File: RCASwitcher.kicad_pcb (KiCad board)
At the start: 2 copper layers, 11 parts, among them J1 Connector_RCA_2x3_REB, J2 Connector_RCA_2x3_REB, J3 Connector_RCA_2x3_REB, J4 Connector_RCA_2x3_REB, J5 Connector_RCA_2x3_REB, J6 Connector_RCA_2x3_REB, SW1 SW_SPDT_3x2_REB, SW2 SW_SPDT_3x2_REB, SW3 SW_SPDT_3x2_REB, SW4 SW_SPDT_3x2_REB, SW5 SW_SPDT_3x2_REB

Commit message: Removing ignored files, some layout
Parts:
- J1, J3, J6: moved to B.Cu
- moved J1 216.2 mm to (49.2, 86.5), turned to 180 degrees
- moved J4 169.1 mm to (99.8, 74.5)
- moved J2 160.8 mm to (56.8, 74.5)
- moved J6 128.2 mm to (135.2, 86.5), turned to 180 degrees
- moved J3 123.3 mm to (92.2, 86.5), turned to 180 degrees
- moved J5 69.1 mm to (142.8, 74.5)
- moved SW4 24.6 mm to (108.8, 138.0)
- moved SW5 24.5 mm to (124.8, 138.0)
- moved SW3 24.1 mm to (93.8, 138.0)
- moved SW2 23.4 mm to (78.8, 138.0)
- moved SW1 23.1 mm to (63.8, 138.0)
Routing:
- net /GND_out: track 0.00 -> 133.4 mm
- net /L_out: track 0.00 -> 133.2 mm
- net Net-(J1-Pad7): track 0.00 -> 131.3 mm
- net /Y_out: track 0.00 -> 131.0 mm
- net Net-(J3-Pad7): track 0.00 -> 112.8 mm
- net /Pb_out: track 0.00 -> 111.1 mm
- net /R_out: track 0.00 -> 110.7 mm
- net Net-(J1-Pad4): track 0.00 -> 109.5 mm
- net Net-(J2-Pad4): track 0.00 -> 103.9 mm, vias 0 -> 1
- net Net-(J1-Pad1): track 0.00 -> 103.2 mm
- net /Pr_out: track 0.00 -> 95.3 mm
- net Net-(J3-Pad4): track 0.00 -> 92.1 mm
- net Net-(J2-Pad1): track 0.00 -> 88.4 mm, vias 0 -> 1
- net Net-(J3-Pad1): track 0.00 -> 86.1 mm
- net Net-(J1-Pad5): track 0.00 -> 85.4 mm, vias 0 -> 1
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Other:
- board outline added: 128.5 x 75.5 mm

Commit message: finish hookups
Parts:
- J5: moved to B.Cu
- J6: moved to F.Cu
- moved J5 14.2 mm to (135.2, 86.5), turned to 180 degrees
- moved J6 14.2 mm to (142.8, 74.5), turned to 0 degrees
- moved SW5 1.00 mm to (123.8, 138.0)
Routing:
- net Net-(J4-Pad4): track 0.00 -> 90.6 mm, vias 0 -> 1
- net Net-(J4-Pad1): track 0.00 -> 74.2 mm, vias 0 -> 1
- net Net-(J5-Pad1): track 0.00 -> 70.9 mm
- net Net-(J4-Pad5): track 0.00 -> 69.0 mm, vias 0 -> 1
- net Net-(J5-Pad4): track 0.00 -> 62.5 mm
- net Net-(J4-Pad2): track 0.00 -> 59.0 mm, vias 0 -> 1
- net Net-(J5-Pad2): track 0.00 -> 53.1 mm
- net /Pr_out: track 95.3 -> 145.1 mm
- net Net-(J4-Pad7): track 28.0 -> 77.4 mm
- net Net-(J4-Pad3): track 0.00 -> 46.7 mm, vias 0 -> 1
- net Net-(J5-Pad5): track 0.00 -> 44.7 mm
- net Net-(J5-Pad3): track 0.00 -> 41.8 mm
- net Net-(J5-Pad7): track 28.0 -> 65.4 mm
- net /Pb_out: track 111.1 -> 130.7 mm
- net /R_out: track 110.7 -> 119.4 mm
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
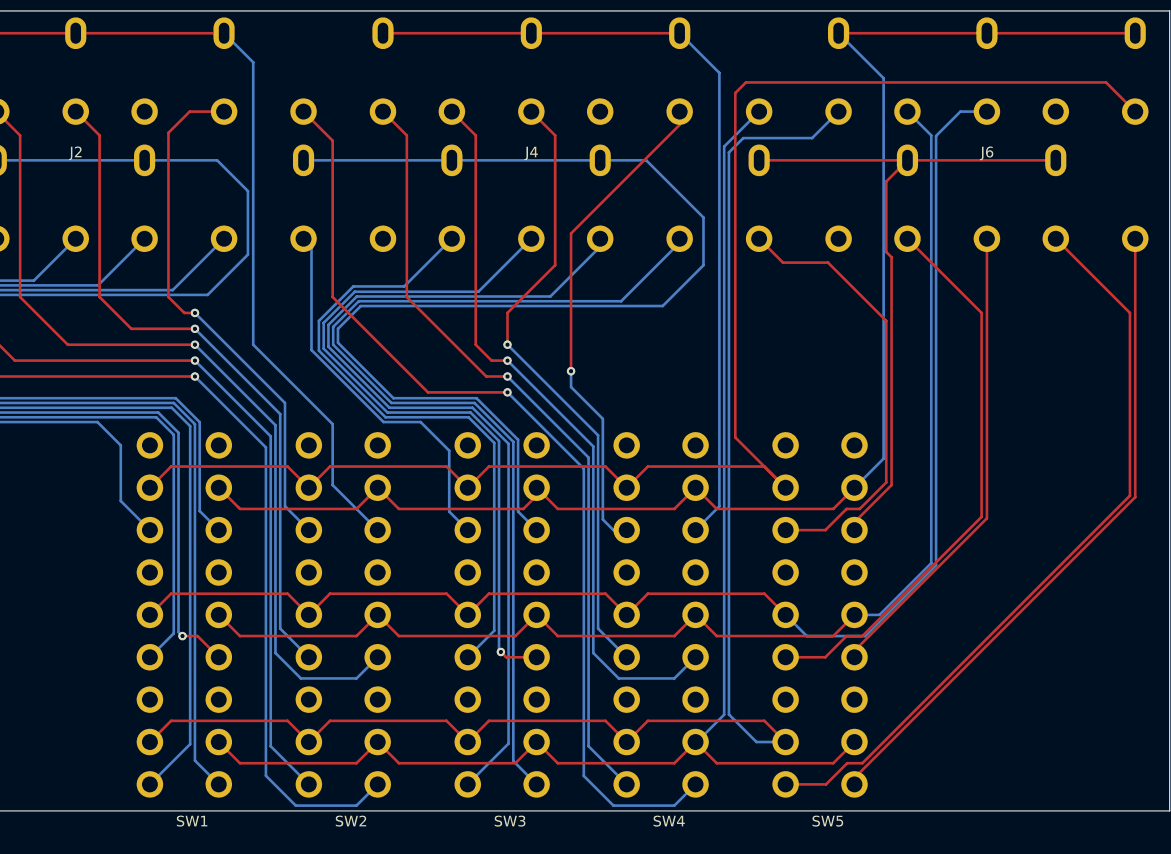
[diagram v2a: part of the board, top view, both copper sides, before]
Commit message: Name remaining nets for checking
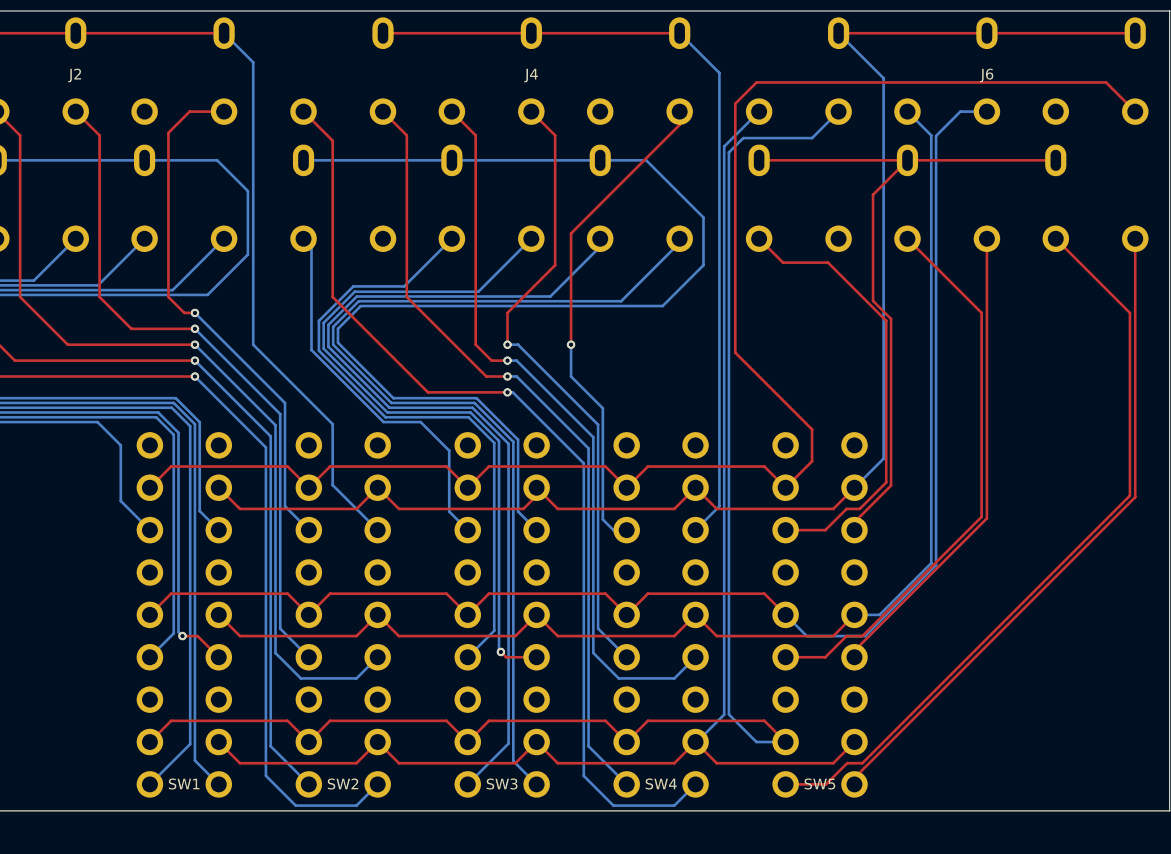
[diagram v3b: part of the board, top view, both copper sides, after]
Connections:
- net Net-(J1-Pad1) renamed /Y_1
- net Net-(J1-Pad2) renamed /Pb_1
- net Net-(J1-Pad3) renamed /Pr_1
- net Net-(J1-Pad4) renamed /L_1
- net Net-(J1-Pad5) renamed /R_1
- net Net-(J1-Pad7) renamed /GND_1
- net Net-(J2-Pad1) renamed /Y_2
- net Net-(J2-Pad2) renamed /Pb_2
- net Net-(J2-Pad3) renamed /Pr_2
- net Net-(J2-Pad4) renamed /L_2
- net Net-(J2-Pad5) renamed /R_2
- net Net-(J2-Pad7) renamed /GND_2
- net Net-(J3-Pad1) renamed /Y_3
- net Net-(J3-Pad2) renamed /Pb_3
- net Net-(J3-Pad3) renamed /Pr_3
- net Net-(J3-Pad4) renamed /L_3
- net Net-(J3-Pad5) renamed /R_3
- net Net-(J3-Pad7) renamed /GND_3
- net Net-(J4-Pad1) renamed /Y_4
- net Net-(J4-Pad2) renamed /Pb_4
- net Net-(J4-Pad3) renamed /Pr_4
- net Net-(J4-Pad4) renamed /L_4
- net Net-(J4-Pad5) renamed /R_4
- net Net-(J4-Pad7) renamed /GND_4
- net Net-(J5-Pad1) renamed /Y_5
- net Net-(J5-Pad2) renamed /Pb_5
- net Net-(J5-Pad3) renamed /Pr_5
- net Net-(J5-Pad4) renamed /L_5
- net Net-(J5-Pad5) renamed /R_5
- net Net-(J5-Pad7) renamed /GND_5
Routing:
- net /Pr_out: track 145.1 -> 146.6 mm
- net /GND_5: track 65.4 -> 66.4 mm
- net /Pb_4: track 59.0 -> 59.5 mm
- net /Y_4: track 74.2 -> 74.7 mm
- net /R_4: track 69.0 -> 69.5 mm

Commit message: Adds notes, one big mistake with switch must fix
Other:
- board text added: "Check whether upper or lower pad is NC when off! Designed with front = ON back = OFF OH NO! front = OFF back = ON Must redo this"
- board text added: "Double check pin assignments in correct orientations Towards front is upside down"
- board text added: "Print out and test spacing on paper!"
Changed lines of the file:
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@@
   )
   (gr_rect (start 31.5 65) (end 160 140.5) (layer "Edge.Cuts") (width 0.1) (fill none))
+  (gr_text "Print out and test spacing on paper!" (at 36.5 58) (layer "User.1")
+    (effects (font (size 1 1) (thickness 0.15)) (justify left))
+  )
+  (gr_text "Double check pin assignments in correct orientations\nTowards front is upside down" (at 33.5 83) (layer "User.1")
+    (effects (font (size 1 1) (thickness 0.15)) (justify left))
+  )
+  (gr_text "Check whether upper or lower\npad is NC when off!\nDesigned with front = ON back = OFF\nOH NO! front = OFF back = ON\nMust redo this" (at 60 134) (layer "User.1")
+    (effects (font (size 1 1) (thickness 0.15)) (justify right))
+  )
   (segment (start 39.359188 102.45) (end 65.813604 102.45) (width 0.25) (layer "B.Cu") (net 1))
   (segment (start 67.55 104.186396) (end 67.55 134.2) (width 0.25) (layer "B.Cu") (net 1))

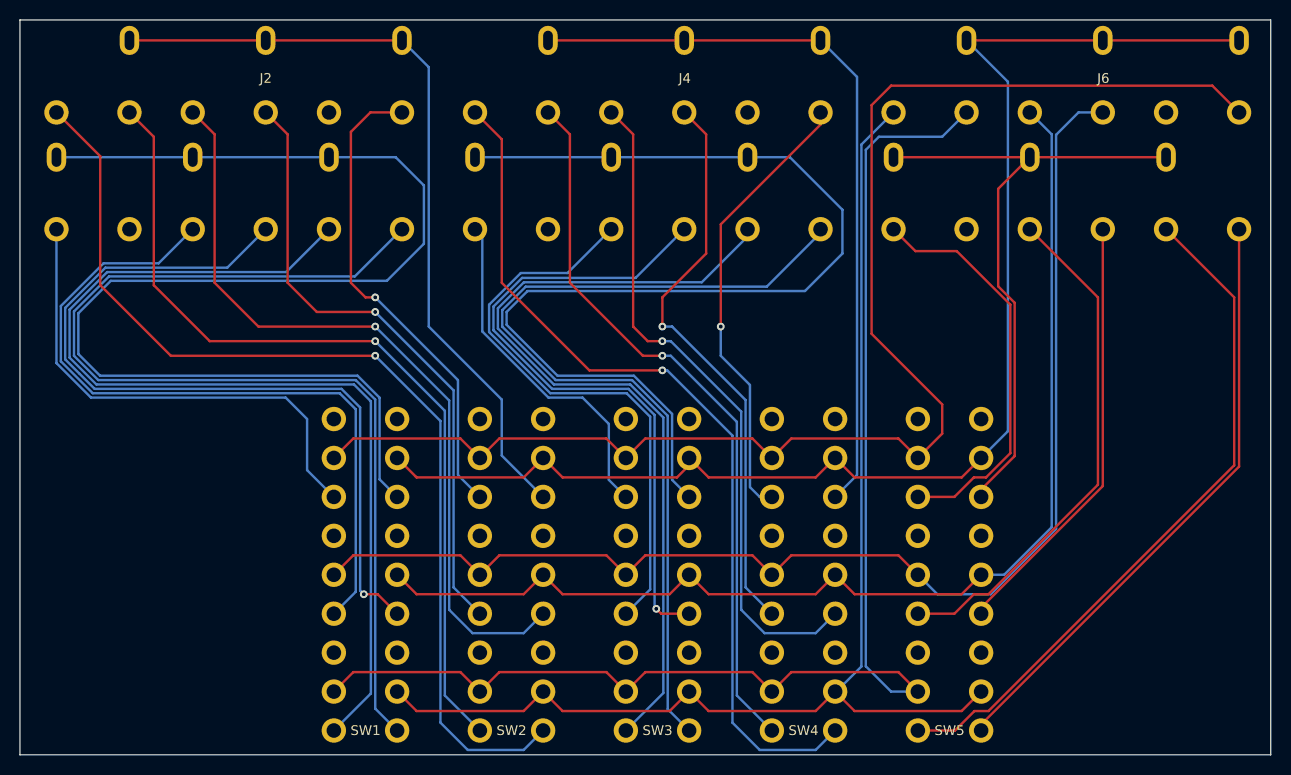
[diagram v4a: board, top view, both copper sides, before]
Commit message: Reversing which side gets connected, tested with hand soldering
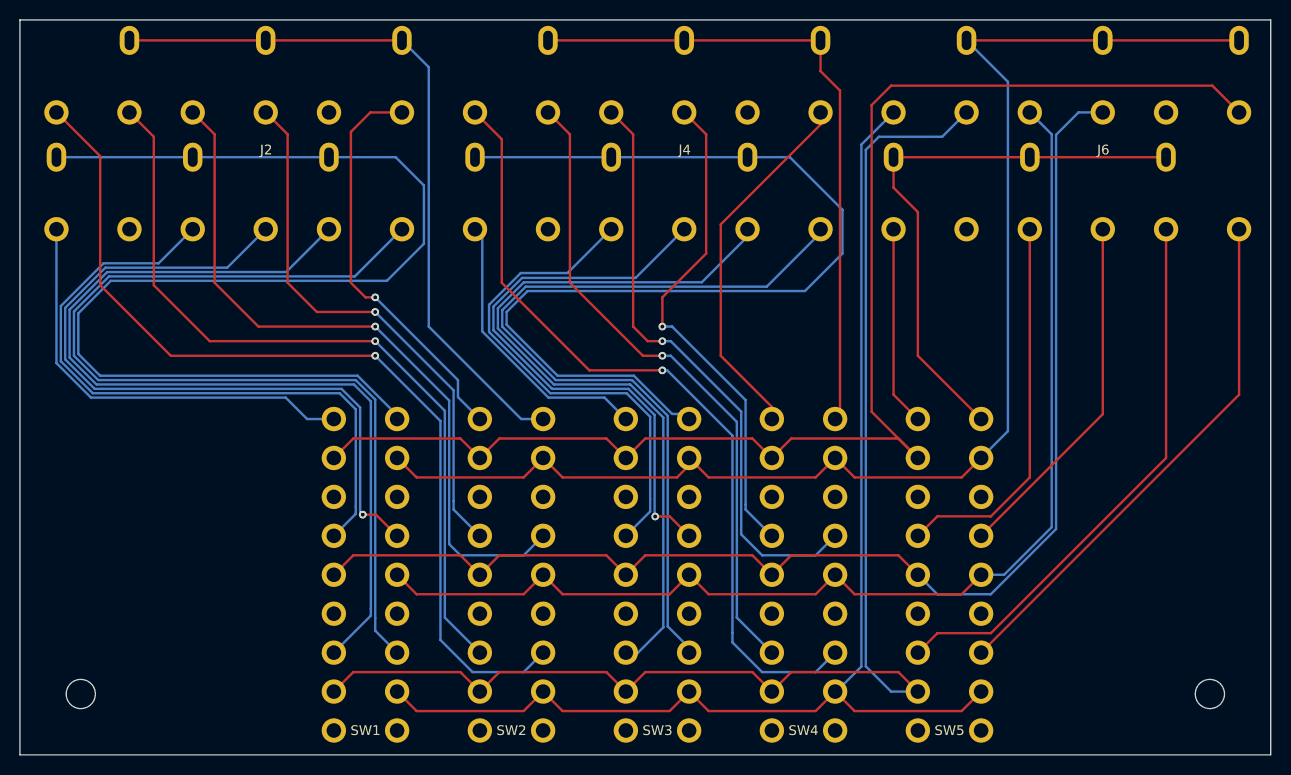
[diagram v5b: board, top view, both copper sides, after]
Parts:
- added REF**: MountingHole_3mm, MountingHole:MountingHole_3mm, F.Cu at (37.8, 134.2)
- added REF**: MountingHole_3mm, MountingHole:MountingHole_3mm, F.Cu at (153.8, 134.2)
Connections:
- SW1 pad 1: /Y_1 -> unconnected-(SW1-Pad1)
- SW1 pad 10: /L_1 -> unconnected-(SW1-Pad10)
- SW1 pad 12: unconnected-(SW1-Pad12) -> /L_1
- SW1 pad 13: /R_1 -> unconnected-(SW1-Pad13)
- SW1 pad 15: unconnected-(SW1-Pad15) -> /R_1
- SW1 pad 16: /GND_1 -> unconnected-(SW1-Pad16)
- SW1 pad 18: unconnected-(SW1-Pad18) -> /GND_1
- SW1 pad 3: unconnected-(SW1-Pad3) -> /Y_1
- SW1 pad 4: /Pb_1 -> unconnected-(SW1-Pad4)
- SW1 pad 6: unconnected-(SW1-Pad6) -> /Pb_1
- SW1 pad 7: /Pr_1 -> unconnected-(SW1-Pad7)
- SW1 pad 9: unconnected-(SW1-Pad9) -> /Pr_1
- SW2 pad 1: /Y_2 -> unconnected-(SW2-Pad1)
- SW2 pad 10: /L_2 -> unconnected-(SW2-Pad10)
- SW2 pad 12: unconnected-(SW2-Pad12) -> /L_2
- SW2 pad 13: /R_2 -> unconnected-(SW2-Pad13)
- SW2 pad 15: unconnected-(SW2-Pad15) -> /R_2
- SW2 pad 16: /GND_2 -> unconnected-(SW2-Pad16)
- SW2 pad 18: unconnected-(SW2-Pad18) -> /GND_2
- SW2 pad 3: unconnected-(SW2-Pad3) -> /Y_2
- SW2 pad 4: /Pb_2 -> unconnected-(SW2-Pad4)
- SW2 pad 6: unconnected-(SW2-Pad6) -> /Pb_2
- SW2 pad 7: /Pr_2 -> unconnected-(SW2-Pad7)
- SW2 pad 9: unconnected-(SW2-Pad9) -> /Pr_2
- SW3 pad 1: /Y_3 -> unconnected-(SW3-Pad1)
- SW3 pad 10: /L_3 -> unconnected-(SW3-Pad10)
- SW3 pad 12: unconnected-(SW3-Pad12) -> /L_3
- SW3 pad 13: /R_3 -> unconnected-(SW3-Pad13)
- SW3 pad 15: unconnected-(SW3-Pad15) -> /R_3
- SW3 pad 16: /GND_3 -> unconnected-(SW3-Pad16)
- SW3 pad 18: unconnected-(SW3-Pad18) -> /GND_3
- SW3 pad 3: unconnected-(SW3-Pad3) -> /Y_3
- SW3 pad 4: /Pb_3 -> unconnected-(SW3-Pad4)
- SW3 pad 6: unconnected-(SW3-Pad6) -> /Pb_3
- SW3 pad 7: /Pr_3 -> unconnected-(SW3-Pad7)
- SW3 pad 9: unconnected-(SW3-Pad9) -> /Pr_3
- SW4 pad 1: /Y_4 -> unconnected-(SW4-Pad1)
- SW4 pad 10: /L_4 -> unconnected-(SW4-Pad10)
- SW4 pad 12: unconnected-(SW4-Pad12) -> /L_4
- SW4 pad 13: /R_4 -> unconnected-(SW4-Pad13)
- SW4 pad 15: unconnected-(SW4-Pad15) -> /R_4
- SW4 pad 16: /GND_4 -> unconnected-(SW4-Pad16)
- SW4 pad 18: unconnected-(SW4-Pad18) -> /GND_4
- SW4 pad 3: unconnected-(SW4-Pad3) -> /Y_4
- SW4 pad 4: /Pb_4 -> unconnected-(SW4-Pad4)
- SW4 pad 6: unconnected-(SW4-Pad6) -> /Pb_4
- SW4 pad 7: /Pr_4 -> unconnected-(SW4-Pad7)
- SW4 pad 9: unconnected-(SW4-Pad9) -> /Pr_4
- SW5 pad 1: /Y_5 -> unconnected-(SW5-Pad1)
- SW5 pad 10: /L_5 -> unconnected-(SW5-Pad10)
- SW5 pad 12: unconnected-(SW5-Pad12) -> /L_5
- SW5 pad 13: /R_5 -> unconnected-(SW5-Pad13)
- SW5 pad 15: unconnected-(SW5-Pad15) -> /R_5
- SW5 pad 16: /GND_5 -> unconnected-(SW5-Pad16)
- SW5 pad 18: unconnected-(SW5-Pad18) -> /GND_5
- SW5 pad 3: unconnected-(SW5-Pad3) -> /Y_5
- SW5 pad 4: /Pb_5 -> unconnected-(SW5-Pad4)
- SW5 pad 6: unconnected-(SW5-Pad6) -> /Pb_5
- SW5 pad 7: /Pr_5 -> unconnected-(SW5-Pad7)
- SW5 pad 9: unconnected-(SW5-Pad9) -> /Pr_5
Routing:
- net /Pr_5: track 41.8 -> 20.5 mm
- net /Pb_5: track 53.1 -> 39.5 mm
- net /Y_5: track 70.9 -> 57.3 mm
- net /GND_4: track 77.4 -> 67.9 mm
- net /R_3: track 69.1 -> 60.2 mm
- net /Pr_4: track 46.7 -> 37.9 mm, vias 1 -> 0
- net /L_2: track 103.9 -> 95.6 mm
- net /L_4: track 90.9 -> 82.7 mm
- net /R_1: track 85.2 -> 77.1 mm
- net /Pb_1: track 76.8 -> 68.8 mm
- net /Pb_4: track 59.5 -> 51.5 mm
- net /Pb_2: track 64.1 -> 56.1 mm
- net /Y_4: track 74.7 -> 66.7 mm
- net /R_5: track 44.7 -> 36.7 mm
- net /Pr_2: track 49.7 -> 41.7 mm
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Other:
- board text removed: "Check whether upper or lower pad is NC when off! Designed with front = ON back = OFF OH NO! front = OFF back = ON Must redo this"
